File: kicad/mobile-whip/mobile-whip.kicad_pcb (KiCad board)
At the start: 2 copper layers, 200 x 22 mm, 55 parts, among them J1 SMA Edge Mount Male, J2 USB_C_Receptacle_USB2.0, Q1 SI2301CDS-T1-GE3, Q2 SI2301CDS-T1-GE3, SW1 MK-12C02-G025, U1 LTC6268IS6, U2 TP4054, U3 LP2985-3.3, U4 TLV431

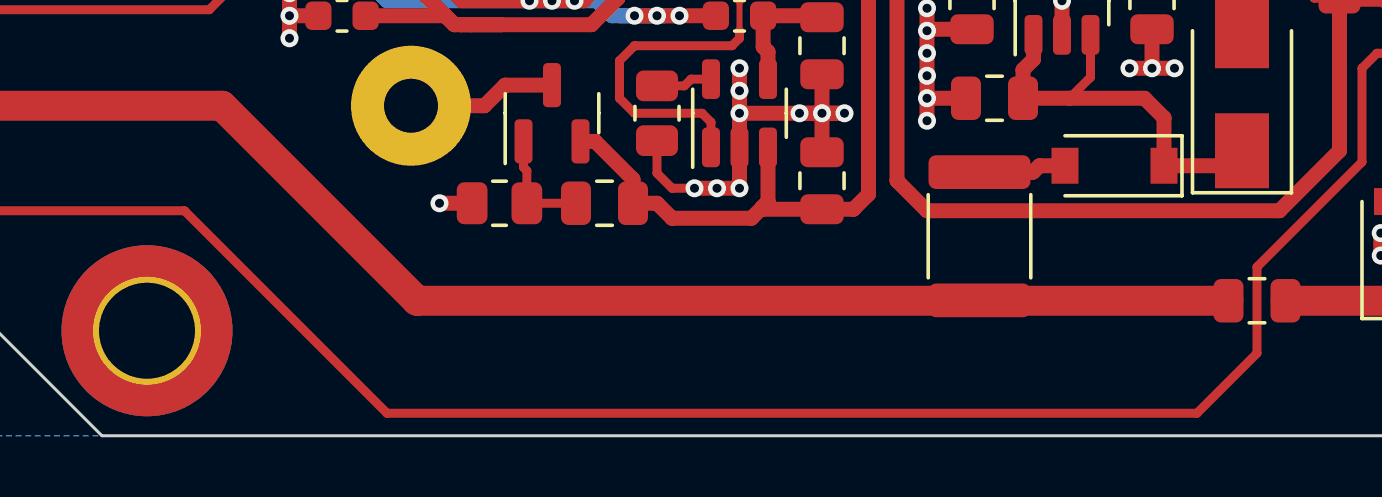
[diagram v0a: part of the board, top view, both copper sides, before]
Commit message: Adjust lithium cell footprint and change red LED resistor to 220R
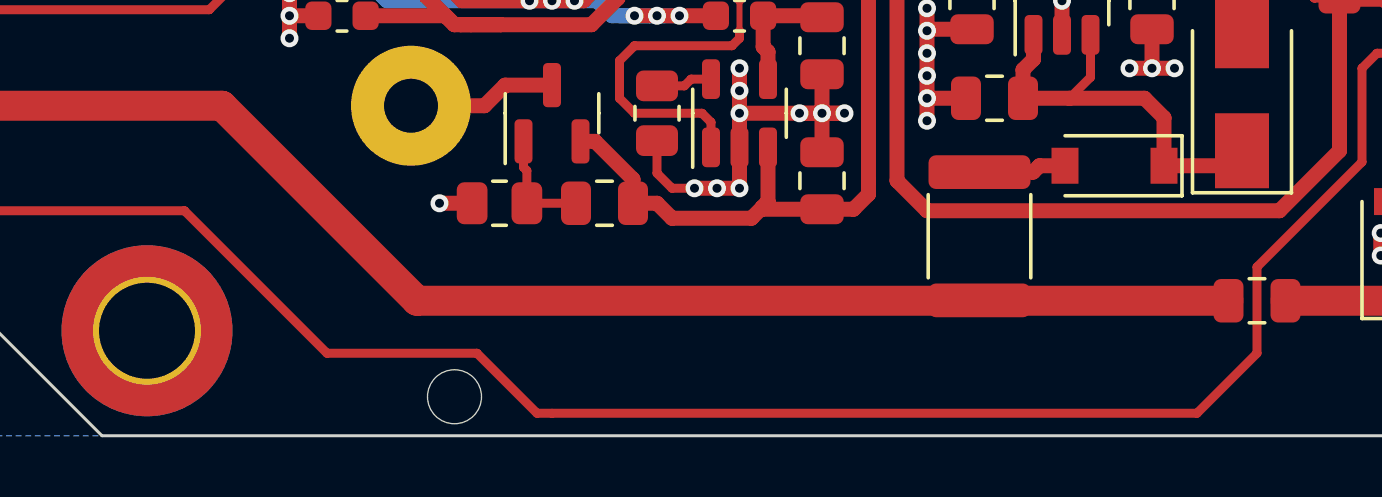
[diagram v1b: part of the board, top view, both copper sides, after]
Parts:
- R11: value 470R -> 220R
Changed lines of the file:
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@@
       (effects (font (size 1 1) (thickness 0.15)))
     )
-    (fp_text value "470R" (at 0 1.65) (layer "F.Fab") hide
+    (fp_text value "220R" (at 0 1.65) (layer "F.Fab") hide
       (effects (font (size 1 1) (thickness 0.15)))
     )
@@
       (effects (font (size 1 1) (thickness 0.15)) (justify mirror))
     )
+    (fp_line (start 10.5 -37.5) (end -10.5 -37.5) (layer "B.SilkS") (width 0.2))
+    (fp_line (start 10.5 -37.5) (end 10.5 37.5) (layer "B.SilkS") (width 0.2))
+    (fp_line (start -10.5 37.5) (end -10.5 -37.5) (layer "B.SilkS") (width 0.2))
     (fp_line (start -10.5 37.5) (end 10.5 37.5) (layer "B.SilkS") (width 0.2))
-    (fp_line (start -10.5 37.5) (end -10.5 -37.5) (layer "B.SilkS") (width 0.2))
-    (fp_line (start 10.5 -37.5) (end 10.5 37.5) (layer "B.SilkS") (width 0.2))
-    (fp_line (start 10.5 -37.5) (end -10.5 -37.5) (layer "B.SilkS") (width 0.2))
     (fp_rect (start -4 18) (end 3.875 20) (layer "B.SilkS") (width 0.1) (fill solid))
     (fp_rect (start -3.9375 -20) (end 3.9375 -18) (layer "B.SilkS") (width 0.1) (fill solid))
     (fp_rect (start -1 23) (end 1 15) (layer "B.SilkS") (width 0.1) (fill solid))
+    (fp_circle (center 0 26.85) (end 1.4 26.85) (layer "B.Fab") (width 0.5) (fill none))
+    (fp_circle (center 0 -26.85) (end 1.4 -26.85) (layer "B.Fab") (width 0.5) (fill none))
+    (pad "" np_thru_hole circle locked (at 9.7 34.25 270) (size 0 0) (drill 1.8) (layers F&B.Cu *.Mask))
     (pad "1" thru_hole circle locked (at 0 35.7 270) (size 4 4) (drill 1.8) (layers *.Cu *.Mask)
       (net 19 "Net-(BT1-Pad1)") (pinfunction "+") (pintype "passive"))
@@
   (segment (start 108 81.875) (end 104.5 85.375) (width 0.3) (layer "F.Cu") (net 18))
   (segment (start 108.5 78.25) (end 108 78.75) (width 0.3) (layer "F.Cu") (net 18))
-  (segment (start 75.5 90.25) (end 68.75 83.5) (width 0.3) (layer "F.Cu") (net 18))
-  (segment (start 102.5 90.25) (end 75.5 90.25) (width 0.3) (layer "F.Cu") (net 18))
   (segment (start 108 78.75) (end 108 81.875) (width 0.3) (layer "F.Cu") (net 18))
   (segment (start 109.3375 78.25) (end 108.5 78.25) (width 0.3) (layer "F.Cu") (net 18))
   (segment (start 68.75 83.5) (end 60 83.5) (width 0.3) (layer "F.Cu") (net 18))
+  (segment (start 73.5 88.25) (end 78.5 88.25) (width 0.3) (layer "F.Cu") (net 18))
   (segment (start 60 83.5) (end 57.25 86.25) (width 0.3) (layer "F.Cu") (net 18))
+  (segment (start 80.5 90.25) (end 81 90.25) (width 0.3) (layer "F.Cu") (net 18))
   (segment (start 104.5 88.25) (end 102.5 90.25) (width 0.3) (layer "F.Cu") (net 18))
+  (segment (start 78.5 88.25) (end 80.5 90.25) (width 0.3) (layer "F.Cu") (net 18))
+  (segment (start 102.5 90.25) (end 81 90.25) (width 0.3) (layer "F.Cu") (net 18))
+  (segment (start 73.5 88.25) (end 68.75 83.5) (width 0.3) (layer "F.Cu") (net 18))
   (via (at 57.25 86.25) (size 0.6) (drill 0.3) (layers "F.Cu" "B.Cu") (net 18))
   (via (at 50.75 86.25) (size 0.6) (drill 0.3) (layers "F.Cu" "B.Cu") (net 18))

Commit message: Remove lowpass capacitors and short input inductor
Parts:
- C3: value 10pF -> N.M.
- C4: value 47pF -> N.M.
- D4, D6: value B5819W SL -> N.M.
- L1: value MLF2012E100KTD25 -> 0R
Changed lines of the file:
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@@
     (property "Sheetfile" "mobile-whip.kicad_sch")
     (property "Sheetname" "")
-    (attr smd)
+    (attr smd exclude_from_pos_files)
     (fp_text reference "C3" (at 0 -1.68) (layer "F.SilkS") hide
       (effects (font (size 1 1) (thickness 0.15)))
     )
-    (fp_text value "10pF" (at 0 1.68) (layer "F.Fab") hide
+    (fp_text value "N.M." (at 0 1.68) (layer "F.Fab") hide
       (effects (font (size 1 1) (thickness 0.15)))
     )
@@
     (property "Sheetfile" "mobile-whip.kicad_sch")
     (property "Sheetname" "")
-    (attr through_hole exclude_from_pos_files)
+    (attr through_hole)
     (fp_text reference "H4" (at -0.508 -2.54 unlocked) (layer "F.SilkS") hide
       (effects (font (size 1 1) (thickness 0.15)))
@@
     (property "Sheetfile" "mobile-whip.kicad_sch")
     (property "Sheetname" "")
-    (attr smd)
+    (attr smd exclude_from_pos_files)
     (fp_text reference "C4" (at 0 -1.68) (layer "F.SilkS") hide
       (effects (font (size 1 1) (thickness 0.15)))
     )
-    (fp_text value "47pF" (at 0 1.68) (layer "F.Fab") hide
+    (fp_text value "N.M." (at 0 1.68) (layer "F.Fab") hide
       (effects (font (size 1 1) (thickness 0.15)))
     )
@@
     (property "Sheetfile" "mobile-whip.kicad_sch")
     (property "Sheetname" "")
-    (attr smd exclude_from_pos_files exclude_from_bom)
+    (attr smd exclude_from_pos_files)
     (fp_text reference "D4" (at 0 -2 90) (layer "F.SilkS") hide
       (effects (font (size 1 1) (thickness 0.15)))
     )
-    (fp_text value "B5819W SL" (at 0 2.1 90) (layer "F.Fab") hide
+    (fp_text value "N.M." (at 0 2.1 90) (layer "F.Fab") hide
       (effects (font (size 1 1) (thickness 0.15)))
     )
@@
       (effects (font (size 1 1) (thickness 0.15)))
     )
-    (fp_text value "MLF2012E100KTD25" (at 0 1.55) (layer "F.Fab") hide
+    (fp_text value "0R" (at 0 1.55) (layer "F.Fab") hide
       (effects (font (size 1 1) (thickness 0.15)))
     )
@@
     (property "Sheetfile" "mobile-whip.kicad_sch")
     (property "Sheetname" "")
-    (attr smd exclude_from_pos_files exclude_from_bom)
+    (attr smd exclude_from_pos_files)
     (fp_text reference "D6" (at 0 -2 90) (layer "F.SilkS") hide
       (effects (font (size 1 1) (thickness 0.15)))
     )
-    (fp_text value "B5819W SL" (at 0 2.1 90) (layer "F.Fab") hide
+    (fp_text value "N.M." (at 0 2.1 90) (layer "F.Fab") hide
       (effects (font (size 1 1) (thickness 0.15)))
     )
@@
     (property "Sheetfile" "mobile-whip.kicad_sch")
     (property "Sheetname" "")
-    (attr through_hole exclude_from_pos_files)
+    (attr through_hole)
     (fp_text reference "H3" (at -0.508 -2.54 unlocked) (layer "F.SilkS") hide
       (effects (font (size 1 1) (thickness 0.15)))
